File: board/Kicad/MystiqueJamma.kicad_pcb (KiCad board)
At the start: 2 copper layers, 140.4 x 114.8 mm, 149 parts, among them IC1 7805, IC10 TDA2030V, IC11 LA4425V, IC2 74HC4021D, IC3 74LS245DW, IC4 74HC4021D, IC5 CY7C1049CV33, IC6 TDA1543T, IC7 74LS245DW, IC8 TLS1233, IC9 74HC4021D, J1 Conn_01x04, J2 Conn_02x10_Odd_Even, J3 FPGA PWR, J4 SDMMC06132, J5 1503_09, J6 HF15H, K1 JAMMA-EDGE-MYSTIQUE

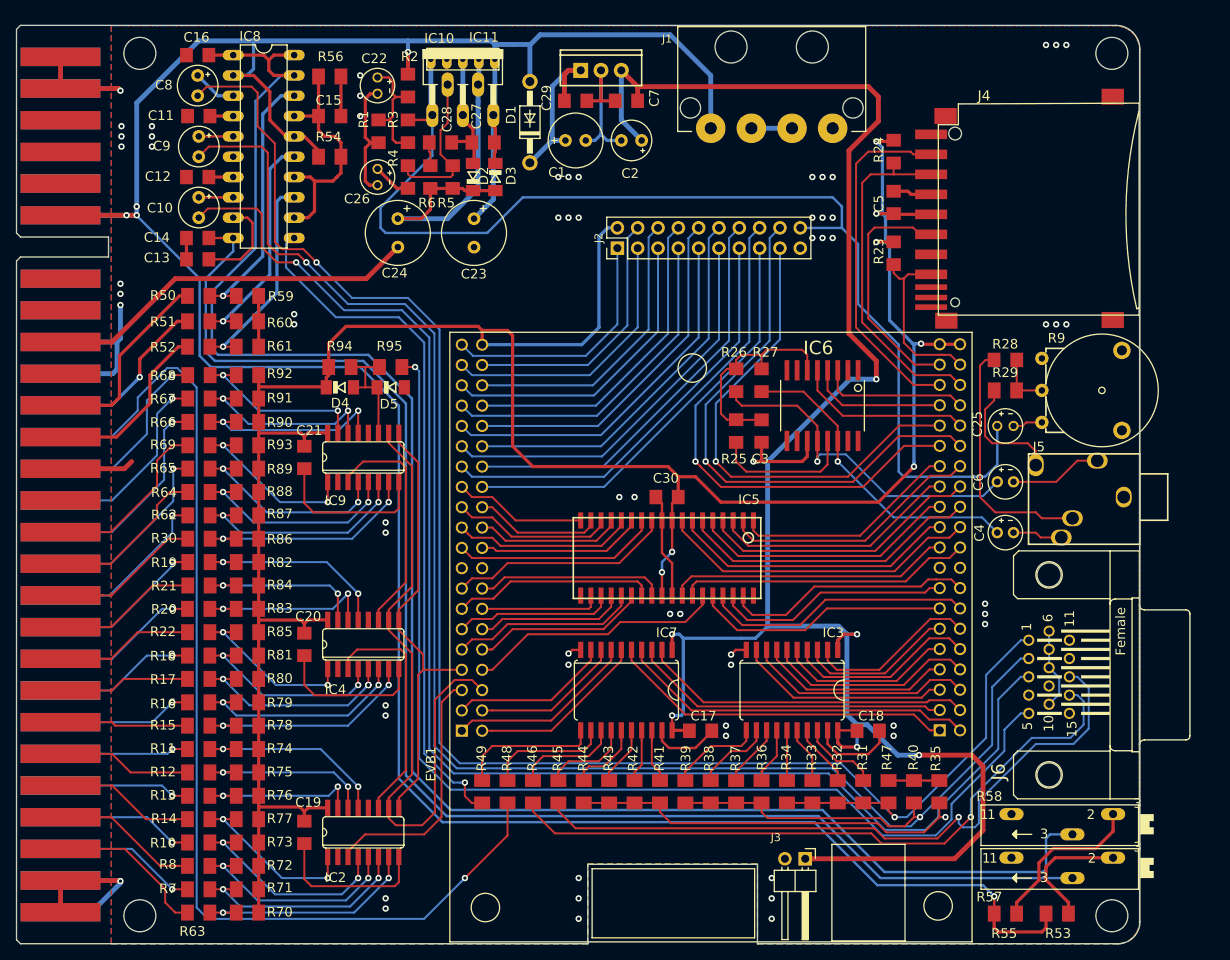
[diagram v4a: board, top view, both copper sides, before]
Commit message: Added Mini DIN6 Connector
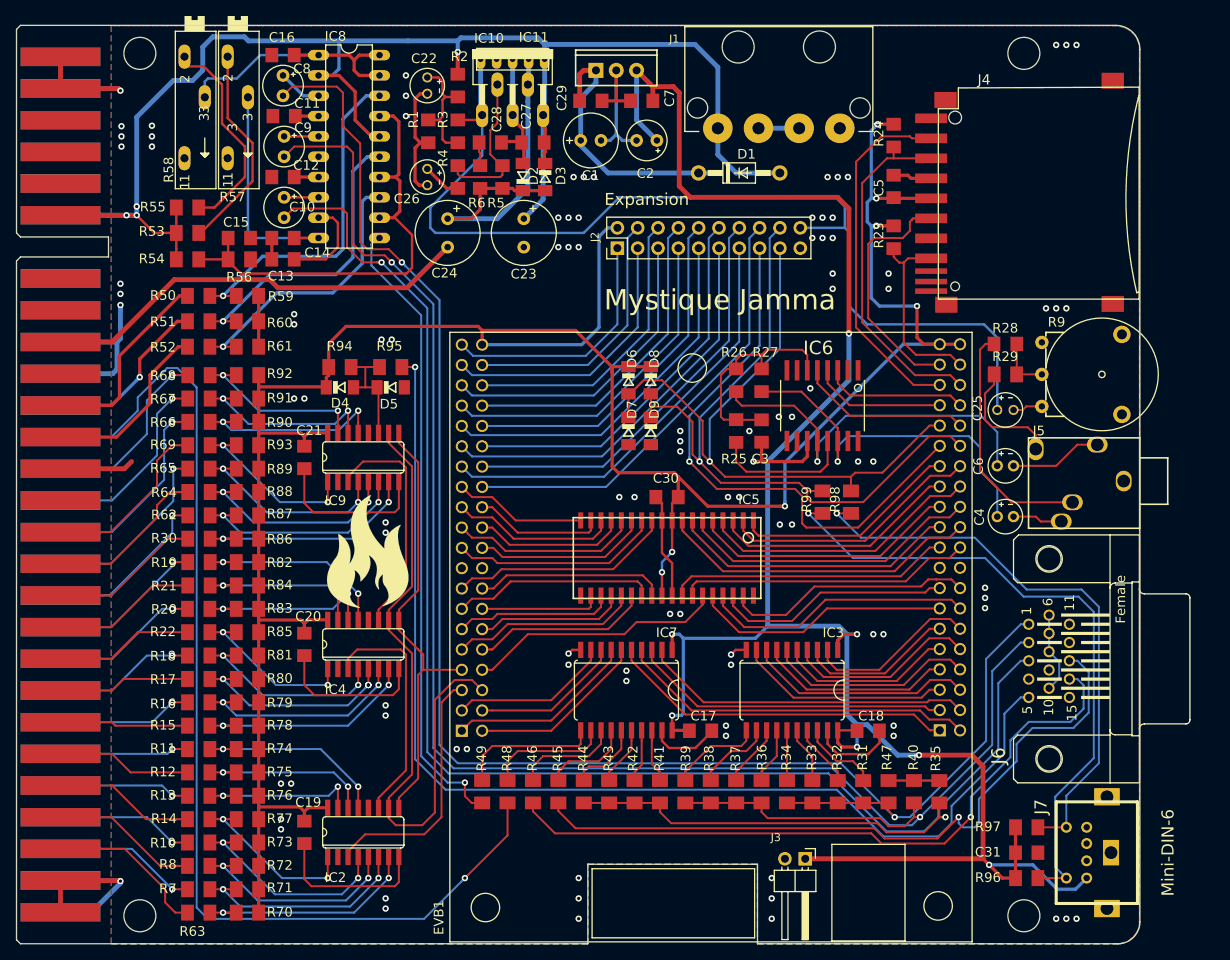
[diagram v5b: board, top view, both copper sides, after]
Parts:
- added C31: 100nF, MystiqueJamma:C1206, F.Cu at (193.2, 135.3)
- added D6: 4148, MystiqueJamma:SOD80C, F.Cu at (143.4, 76.2)
- added D7: 4148, MystiqueJamma:SOD80C, F.Cu at (143.4, 82.5)
- added D8: 4148, MystiqueJamma:SOD80C, F.Cu at (146.2, 76.2)
- added D9: 4148, MystiqueJamma:SOD80C, F.Cu at (146.2, 82.5)
- added G***: LOGO, MystiqueJamma:logo_flames2, F.Cu at (111.0, 97.7)
- added J7: Mini-DIN-6, r_mini_din:Mini_din6, F.Cu at (201.9, 135.3)
- added R96: 2K2, MystiqueJamma:M1206, F.Cu at (193.2, 138.4)
- added R97: 2K2, MystiqueJamma:M1206, F.Cu at (193.2, 132.1)
- added R98: 120, MystiqueJamma:M1206, F.Cu at (171.2, 91.4)
- added R99: 120, MystiqueJamma:M1206, F.Cu at (167.6, 91.4)
- moved R58 139.8 mm to (89.2, 42.7), turned to 270 degrees
- moved R57 139.3 mm to (94.6, 42.7), turned to 270 degrees
- moved R53 138.1 mm to (88.3, 57.8)
- moved R55 135.1 mm to (88.3, 54.6)
- moved D1 26.9 mm to (157.2, 50.3), turned to 0 degrees
- moved R56 25.5 mm to (94.7, 61.1)
- moved R54 21.9 mm to (88.3, 61.1)
- moved C15 19.0 mm to (94.7, 58.4)
- moved C10 10.7 mm to (100.3, 54.6)
- moved C11 10.7 mm to (100.3, 43.2)
- moved C12 10.7 mm to (100.2, 50.8)
- moved C13 10.7 mm to (100.2, 61.1)
- moved C14 10.7 mm to (100.2, 58.4)
- moved C16 10.7 mm to (100.2, 35.6)
- moved C8 10.7 mm to (100.2, 39.4)
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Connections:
- net /COIN_CT1 renamed Net-(K1-Pad8)
- net /COIN_CT2 renamed Net-(K1-PadJ)
- net /IO_111 renamed PS2CK
- net /IO_114 renamed PS2DAT
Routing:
- net Net-(C16-Pad1): track 221.4 -> 33.3 mm
- net +12V: track 367.1 -> 196.0 mm, vias 5 -> 4
- net Net-(C14-Pad1): track 181.5 -> 28.9 mm
- net Net-(J7-Pad6): track 0.00 -> 82.0 mm, vias 0 -> 1
- net Net-(J7-Pad1): track 0.00 -> 72.2 mm, vias 0 -> 1
- net Net-(C15-Pad1): track 30.1 -> 57.6 mm
- net PS2CK: track 61.4 -> 84.8 mm
- net PS2DAT: track 68.8 -> 88.7 mm
- net /AUD-IN: track 147.2 -> 129.5 mm
- net +5V: track 250.9 -> 265.2 mm, vias 7 -> 8
- net Net-(C1-Pad+): track 22.3 -> 32.9 mm
- net Net-(R53-Pad1): track 15.9 -> 26.3 mm
- net Net-(IC8-Pad18): track 32.8 -> 42.6 mm
- net Net-(IC8-Pad15): track 28.4 -> 37.7 mm
- net /BURST_GATE: track 87.6 -> 78.9 mm
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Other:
- board text added: "Expansion"
- board text added: "Mystique Jamma"

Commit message: Added Logo, arranged component labels
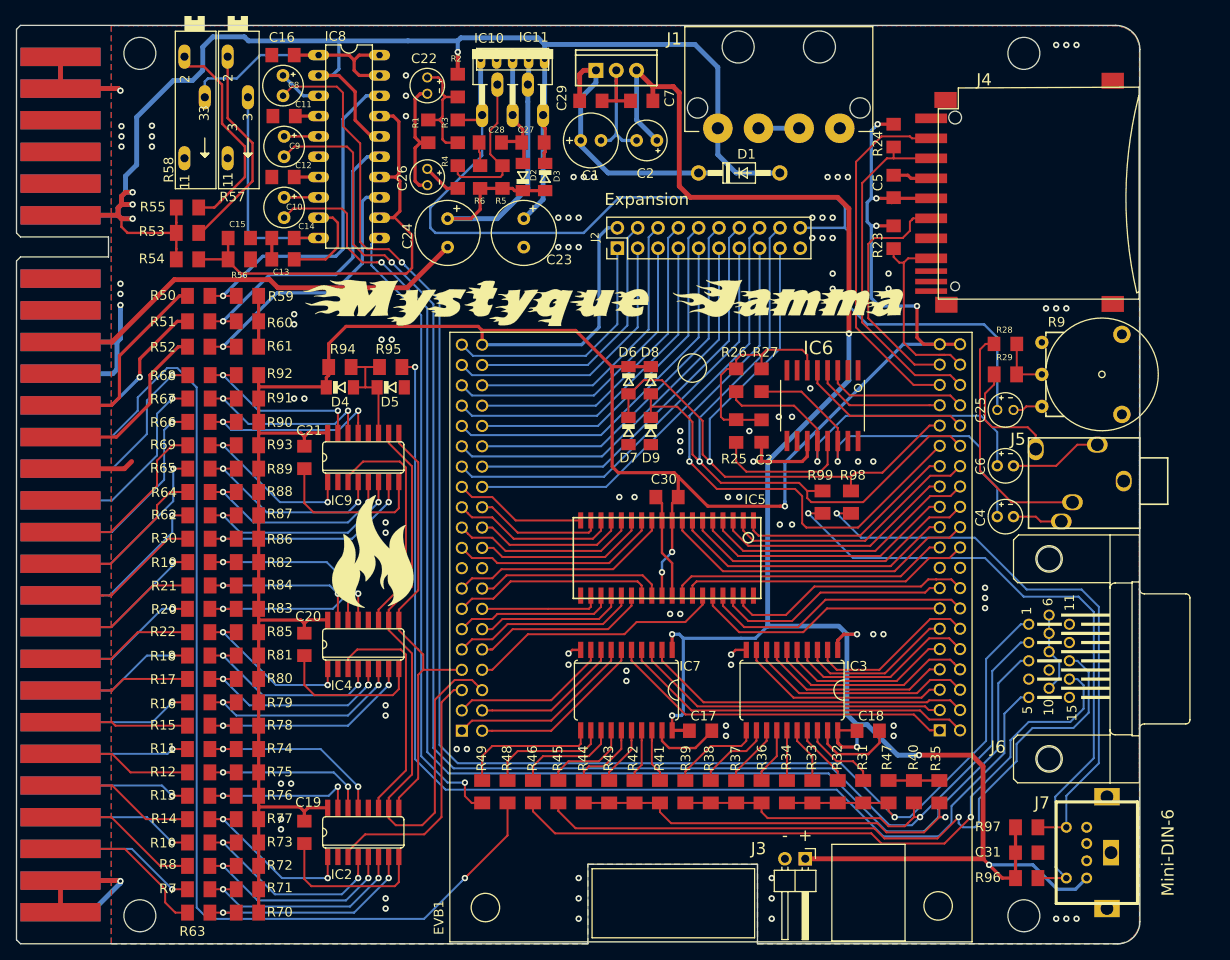
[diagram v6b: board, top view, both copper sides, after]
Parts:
- added G***: LOGO, MystiqueJamma:logotype2, F.Cu at (140.2, 66.5)
- moved G*** 0.63 mm to (111.6, 97.7)
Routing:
- net +12V: track 196.0 -> 206.5 mm
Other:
- board text added: "+"
- board text added: "-"
- board text removed: "Mystique Jamma"

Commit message: Added second SRAM, Match FPGA IO usage with board available pins
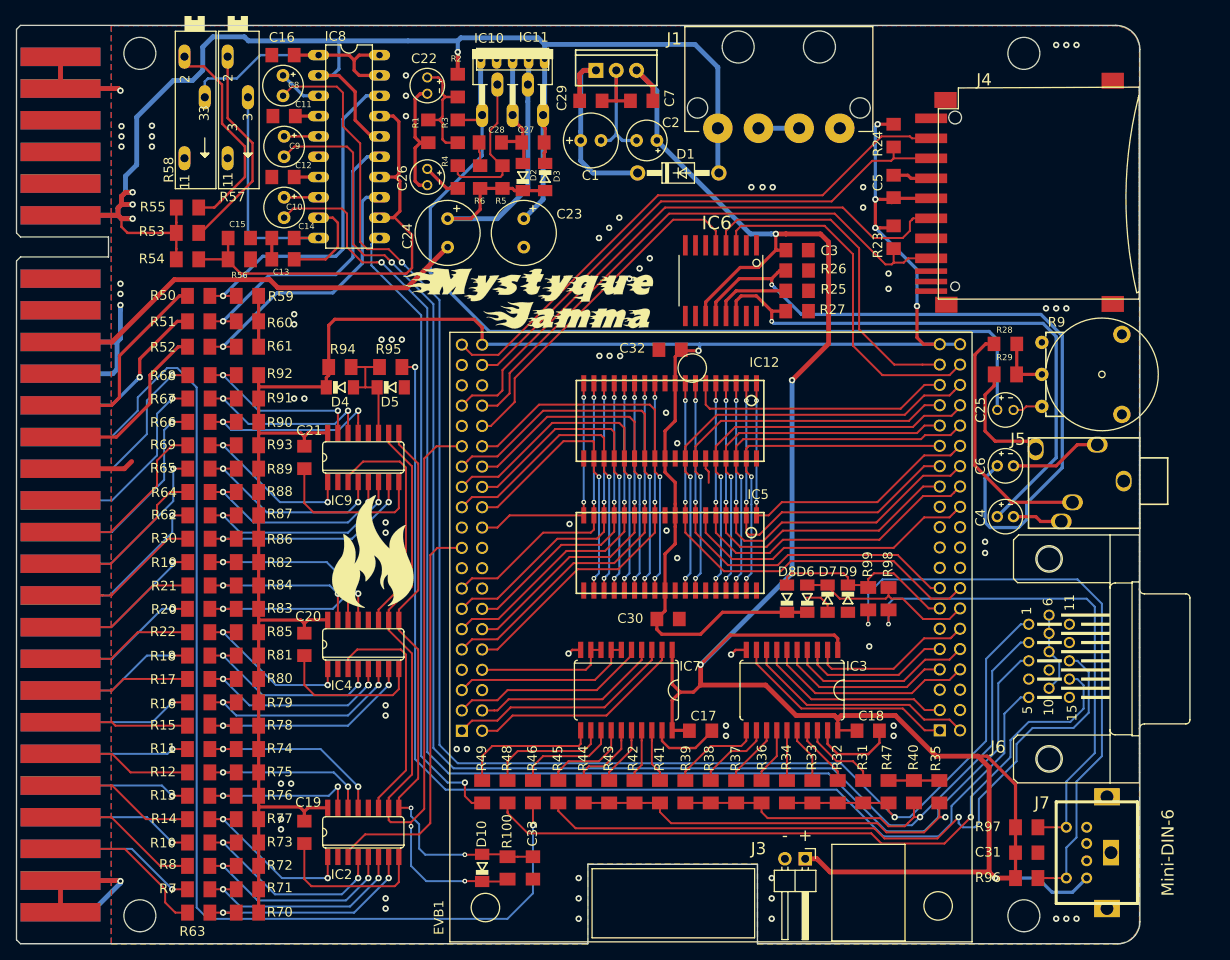
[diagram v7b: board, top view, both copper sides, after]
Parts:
- removed the G*** at (140.2, 66.5)
- removed J2: Conn_02x10_Odd_Even, Connector_PinHeader_2.54mm:PinHeader_2x10_P2.54mm_Vertical
- added C32: 100nF, MystiqueJamma:C1206, F.Cu at (148.6, 72.4)
- added C33: 10n, MystiqueJamma:C1206, F.Cu at (131.4, 137.2)
- added D10: 4148, MystiqueJamma:SOD80C, F.Cu at (125.1, 137.2)
- added G***: LOGO, MystiqueJamma:logoCompact, F.Cu at (131.1, 66.0)
- added IC12: CY7C1049CV33, MystiqueJamma:SOJV36-400, F.Cu at (148.6, 81.3)
- added R100: 4k7, MystiqueJamma:M1206, F.Cu at (128.3, 137.2)
- C22: value CPOL-USE2-4 -> 22u
- C25: value CPOL-USE2-4 -> 10uF
- C26: value CPOL-USE2-4 -> 2u2
- C28: value 100nF -> 220nF
- D2, D3: value DIODE-SOD80C -> 1N4004
- R1, R2, R3: value 470 -> 100k
- R28, R29, R4: value 470 -> 4k7
- R41: value 330 -> 420
- R42: value 330 -> 785
- R43: value 330 -> 1380
- R44: value 330 -> 2230
- R5: value 470 -> 150k
- R53, R54, R55, R70, R71, R72, R73, R74, R75, R76, R77, R78, R79, R80, R81, R82, R83, R84, R85, R86, R87, R88, R89, R90, R91, R92, R93, R94: value 330 -> 10k
- R56: value 330 -> 5k
- R57, R58: value TRIM_EU-B90P -> 5k
- R59, R60, R61: value 330 -> 430
- R6: value 470 -> 1R
- R9: value VOLUME-POT -> 50k
- moved D6 35.3 mm to (165.7, 103.5), turned to 90 degrees
- moved D7 32.5 mm to (168.3, 103.5)
- moved D9 32.3 mm to (170.8, 103.5)
- moved D8 32.2 mm to (163.2, 103.5), turned to 90 degrees
- moved C3 23.0 mm to (164.5, 59.9), turned to 0 degrees
- moved IC6 20.1 mm to (154.9, 63.8)
- moved R25 19.1 mm to (164.5, 65.0), turned to 180 degrees
- moved R26 15.7 mm to (164.5, 62.5), turned to 180 degrees
- moved C30 15.2 mm to (148.3, 106.0), turned to 0 degrees
- moved R99 13.4 mm to (173.4, 103.5)
- moved R98 12.9 mm to (175.9, 103.5)
- moved R27 9.71 mm to (164.5, 67.6), turned to 180 degrees
- moved D1 7.62 mm to (149.6, 50.3)
- moved IC5 0.74 mm to (148.6, 97.8)
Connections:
- net /SRAM_CE renamed /SRAM_CE1
- EVB1 pad I0_1: /G2 -> Net-(EVB1-PadI0_1)
- EVB1 pad I0_10: /B2 -> /G2
- EVB1 pad I0_100: /IO_100 -> /SD_CS
- EVB1 pad I0_101: /SD_SCLK -> /I2S_WS
- EVB1 pad I0_103: /SD_DATAOUT -> /I2S_BCK
- EVB1 pad I0_104: /SD_CS -> /SRAM_CE2
- EVB1 pad I0_105: /SD_DATAIN -> /SRAM_IO6
- EVB1 pad I0_106: /IS2_WS -> /SRAM_IO7
- EVB1 pad I0_11: /B3 -> /G3
- EVB1 pad I0_110: /I2S_BCK -> /SRAM_A15
- EVB1 pad I0_111: PS2CK -> /SRAM_A16
- EVB1 pad I0_112: /I2S_DATA -> /SRAM_A17
- EVB1 pad I0_113: /IO_113 -> /SRAM_A18
- EVB1 pad I0_114: PS2DAT -> /SRAM_A0
- EVB1 pad I0_115: /SRAM_A0 -> /SRAM_A1
- EVB1 pad I0_119: /SRAM_A1 -> /SRAM_A2
- EVB1 pad I0_120: /SRAM_A2 -> /SRAM_A3
- EVB1 pad I0_121: /SRAM_A3 -> /SRAM_A4
- EVB1 pad I0_124: /SRAM_A4 -> Net-(EVB1-PadI0_124)
- EVB1 pad I0_126: /SRAM_IO0 -> Net-(EVB1-PadI0_126)
- EVB1 pad I0_127: /SRAM_IO1 -> Net-(EVB1-PadI0_127)
- EVB1 pad I0_128: /SRAM_IO6 -> Net-(EVB1-PadI0_128)
- EVB1 pad I0_129: /SRAM_IO7 -> Net-(EVB1-PadI0_129)
- EVB1 pad I0_132: /SRAM_A18 -> /SRAM_IO1
- EVB1 pad I0_133: /SRAM_A17 -> /SRAM_IO0
- EVB1 pad I0_135: /SRAM_A16 -> PS2CK
- EVB1 pad I0_136: /SRAM_A15 -> PS2DAT
- EVB1 pad I0_138: /R1 -> Net-(EVB1-PadI0_138)
- EVB1 pad I0_142: /R3 -> /R1
- EVB1 pad I0_144: /G1 -> /R3
- EVB1 pad I0_2: /G3 -> Net-(EVB1-PadI0_2)
- EVB1 pad I0_28: /VSY -> /B1
- EVB1 pad I0_3: /B0 -> Net-(EVB1-PadI0_3)
- EVB1 pad I0_30: /HSY -> /B0
- EVB1 pad I0_31: /GATE -> /B3
- EVB1 pad I0_32: /CSY -> /B2
- EVB1 pad I0_33: /CNTR_DAT -> /HSY
- EVB1 pad I0_34: /CNTR_CLK -> Net-(EVB1-PadI0_34)
- EVB1 pad I0_38: /CNTR_LATCH -> Net-(EVB1-PadI0_38)
- EVB1 pad I0_39: /SRAM_OE -> /VSY
- EVB1 pad I0_42: /SRAM_A13 -> /SRAM_IO3
- EVB1 pad I0_43: /SRAM_A14 -> /SRAM_IO2
- EVB1 pad I0_44: /SRAM_A11 -> /SRAM_A5
- EVB1 pad I0_46: /SRAM_A12 -> /SRAM_WE
- EVB1 pad I0_49: /SRAM_IO4 -> /SRAM_A7
- EVB1 pad I0_50: /SRAM_A10 -> /SRAM_A6
- EVB1 pad I0_51: /SRAM_IO2 -> /SRAM_A8
- EVB1 pad I0_52: /SRAM_IO5 -> Net-(EVB1-PadI0_52)
- EVB1 pad I0_53: /SRAM_IO3 -> /CNTR_DAT
- EVB1 pad I0_54: /SRAM_WE -> Net-(EVB1-PadI0_54)
- EVB1 pad I0_55: /SRAM_A5 -> Net-(EVB1-PadI0_55)
- EVB1 pad I0_58: /SRAM_A6 -> /SRAM_A9
- EVB1 pad I0_59: /SRAM_A7 -> /SRAM_A11
- EVB1 pad I0_60: /SRAM_A8 -> /SRAM_A10
- EVB1 pad I0_64: /SRAM_A9 -> /SRAM_A13
- EVB1 pad I0_65: /IO_65 -> /SRAM_A12
- EVB1 pad I0_66: /IO_66 -> /SRAM_IO4
- EVB1 pad I0_67: /IO_67 -> /SRAM_A14
- EVB1 pad I0_68: /IO_68 -> /CNTR_CK_LAT
- EVB1 pad I0_69: /IO_69 -> /SRAM_IO5
- EVB1 pad I0_7: /B1 -> /G1
- EVB1 pad I0_70: /IO_70 -> Net-(EVB1-PadI0_70)
- EVB1 pad I0_71: /IO_71 -> /I2S_DATA
- EVB1 pad I0_72: /IO_72 -> /SD_CNT_SCLK
- EVB1 pad I0_88: /IO_88 -> /SD_DATAOUT
- EVB1 pad I0_89: /IO_89 -> Net-(EVB1-PadI0_89)
- EVB1 pad I0_90: /IO_90 -> Net-(EVB1-PadI0_90)
- EVB1 pad I0_91: /IO_91 -> Net-(EVB1-PadI0_91)
- EVB1 pad I0_99: /IO_99 -> /SD_DATAIN
- IC2 pad 10: /CNTR_CLK -> /CNTR_CK_LAT
- IC2 pad 9: /CNTR_LATCH -> /LATCH
- IC4 pad 10: /CNTR_CLK -> /CNTR_CK_LAT
- IC4 pad 9: /CNTR_LATCH -> /LATCH
- IC5 pad 31: /SRAM_OE -> GND
- IC6 pad 4: /IS2_WS -> /I2S_WS
- IC7 pad 7: /VSY -> /HSY
- IC7 pad 8: /CSY -> /VSY
- IC7 pad 9: /GATE -> /VSY
- IC9 pad 10: /CNTR_CLK -> /CNTR_CK_LAT
- IC9 pad 9: /CNTR_LATCH -> /LATCH
- J4 pad 5: /SD_SCLK -> /SD_CNT_SCLK
- R46 pad 2: /VGA-VSYNC -> /JAMMA-CSYNC
- R48 pad 2: /JAMMA-CSYNC -> /VGA-VSYNC
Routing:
- net /CNTR_CK_LAT: track 0.00 -> 127.0 mm, vias 0 -> 2
- net /CNTR_CLK: track 81.4 -> 0.00 mm
- net /SD_CNT_SCLK: track 0.00 -> 73.7 mm
- net /LATCH: track 0.00 -> 72.6 mm, vias 0 -> 2
- net /IO_113: track 71.3 -> 0.00 mm, vias 1 -> 0
- net PS2DAT: track 88.7 -> 24.7 mm, vias 1 -> 0
- net PS2CK: track 84.8 -> 22.8 mm, vias 1 -> 0
- net /CNTR_LATCH: track 56.2 -> 0.00 mm
- net /IO_65: track 55.8 -> 0.00 mm
- net /IO_66: track 53.9 -> 0.00 mm
- net /IO_67: track 52.6 -> 0.00 mm
- net /IO_68: track 50.1 -> 0.00 mm
- net /IO_69: track 48.3 -> 0.00 mm
- net /SD_DATAOUT: track 25.1 -> 72.3 mm
- net /IO_70: track 46.3 -> 0.00 mm
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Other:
- net class Default: via_dia 0.8 -> 0.6; via_drill 0.4 -> 0.3
- rule via_min_size: 0.4 -> 0.6
- board text removed: "Expansion"

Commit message: Circuit update and cleanup
Added second SRAM, changed VGA detect to FPGA instead of shift registers, added solder joint to force VGA mode, added RC-Network to Shift Register clock signal to allow same line to control LATCH signal.
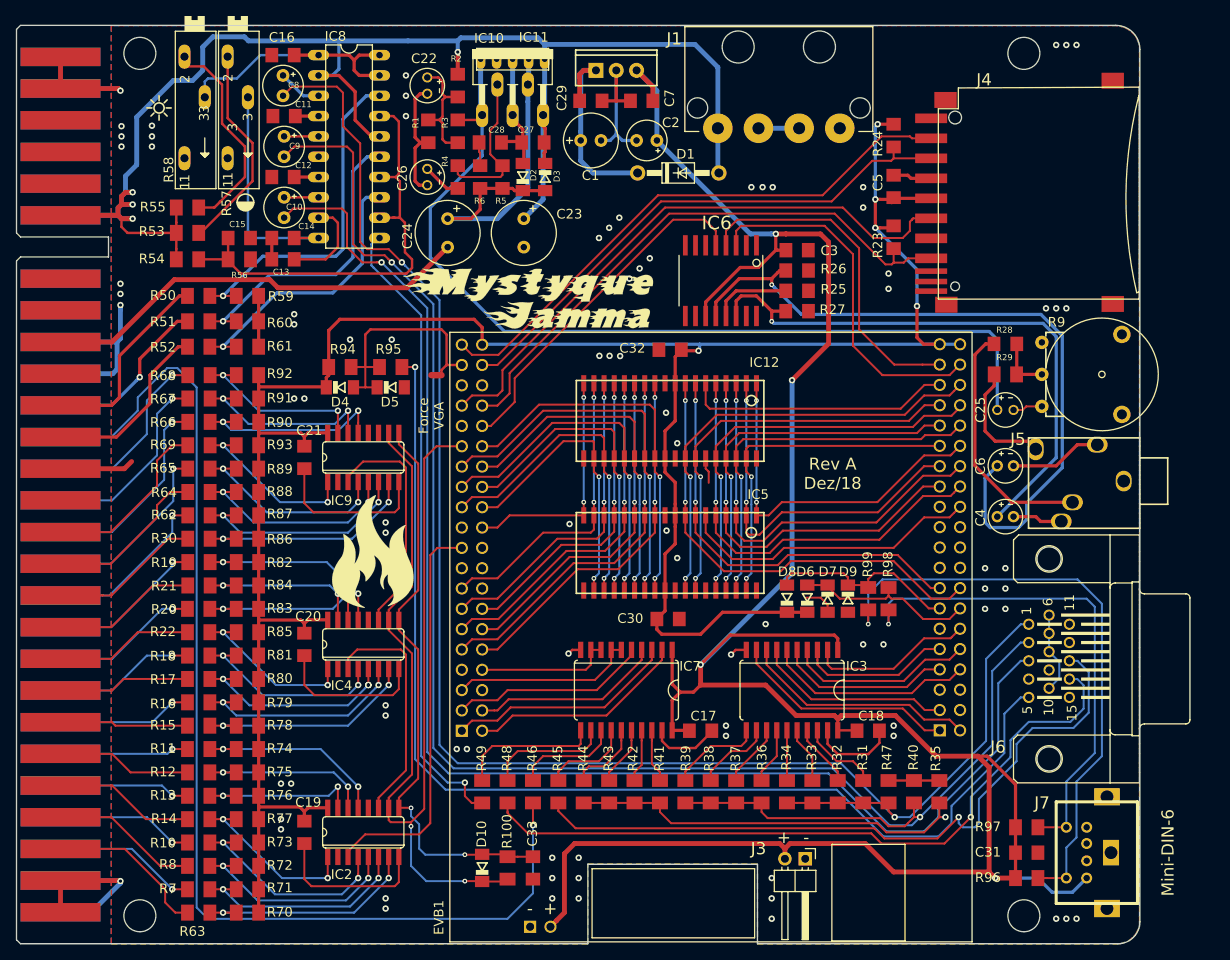
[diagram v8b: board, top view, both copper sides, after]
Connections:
- C33 pad 2: GND -> Net-(C33-Pad2)
- D4 pad A: Net-(D4-PadA) -> /VGA_DET_IN
- D5 pad C: Net-(D4-PadA) -> /VGA_DET_IN
- EVB1 pad I0_91: Net-(EVB1-PadI0_91) -> /VGA_DET_IN
- IC9 pad 11: Net-(D4-PadA) -> GND
- J3 pad 1: +5V -> GND
- J3 pad 2: GND -> +5V
- R94 pad 1: Net-(D4-PadA) -> /VGA_DET_IN
- R95 pad 1: Net-(D4-PadA) -> /VGA_DET_IN
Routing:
- net +5V: track 280.1 -> 323.1 mm
- net /VGA_DET_IN: track 0.00 -> 32.6 mm
- net Net-(D4-PadA): track 14.8 -> 0.00 mm
- net /AUD-IN: track 116.4 -> 115.3 mm
- net GND: vias 81 -> 89
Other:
- board text added: "Force VGA"
- board text added: "Rev A Dez/18"
